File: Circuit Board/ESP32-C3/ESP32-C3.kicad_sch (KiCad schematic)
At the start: 9 parts

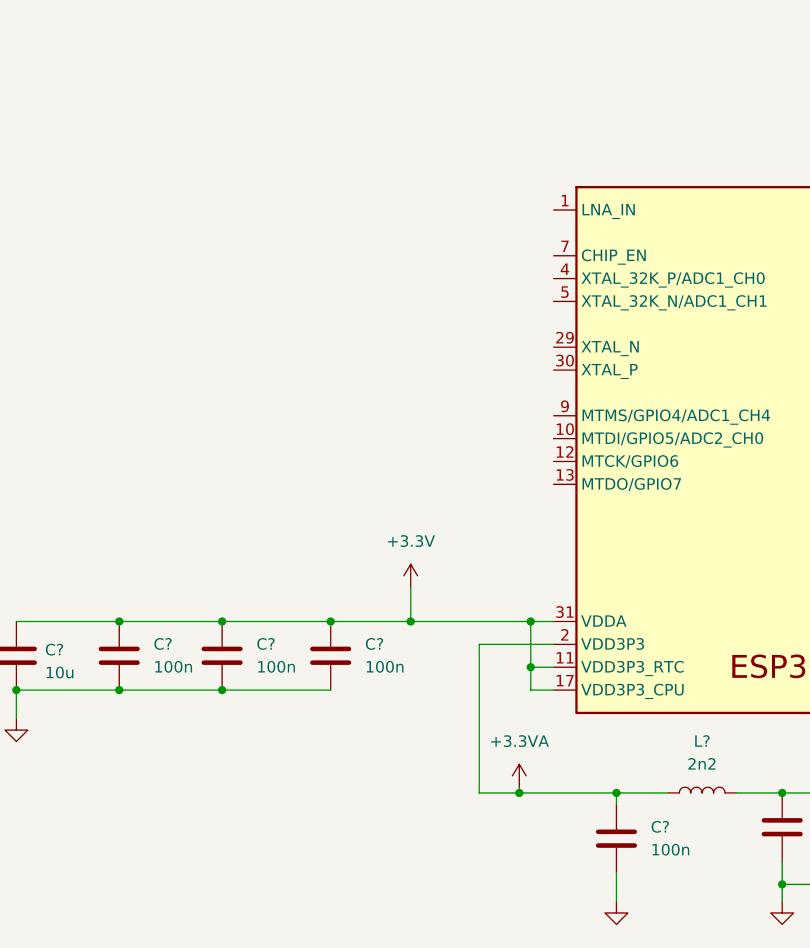
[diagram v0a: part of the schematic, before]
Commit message: Added the crystal oscillator
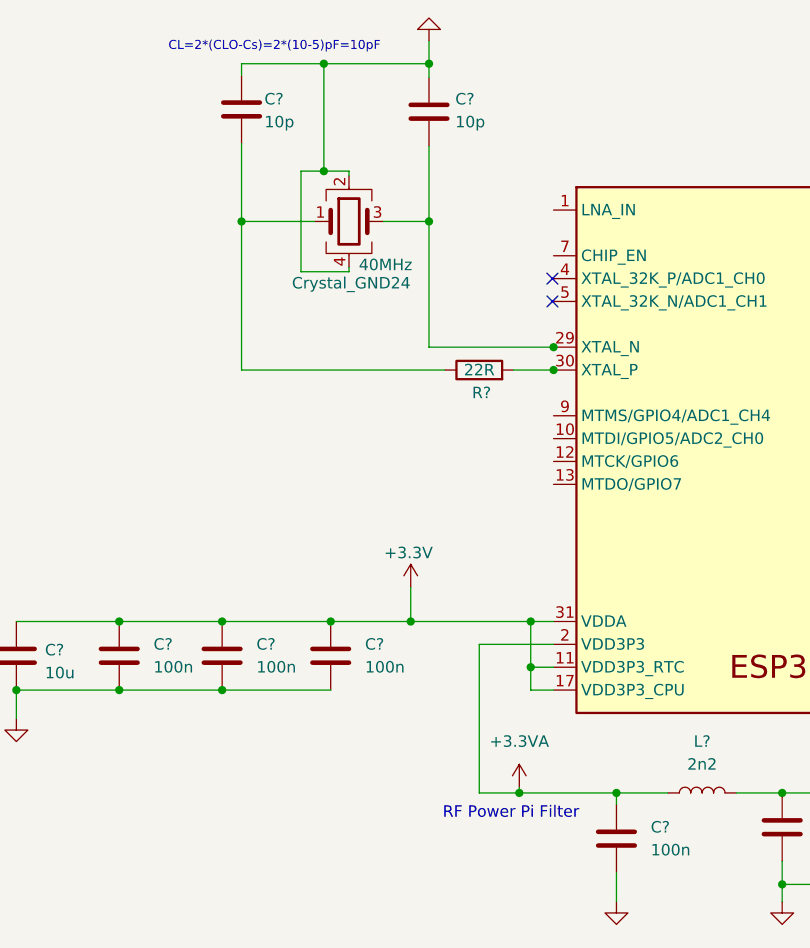
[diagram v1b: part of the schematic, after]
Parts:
- added 40MHz: Crystal_GND24, symbol Device:Crystal_GND24
- added C? (x2): 10p, symbol Device:C
- added R?: 22R, symbol Device:R
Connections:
- net GND: now also 40MHz.2, 40MHz.4, C?.1, C?.1
- net at U?.29 (XTAL_N): now also 40MHz.3, C?.2
- net at U?.30 (XTAL_P): now also R?.2
- new net: 40MHz.1, C?.2, R?.1
- no-connect marks 0 -> 2
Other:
- note added: "CL=2*(CLO-Cs)=2*(10-5)pF=10pF"
- note added: "RF Power Pi Filter"

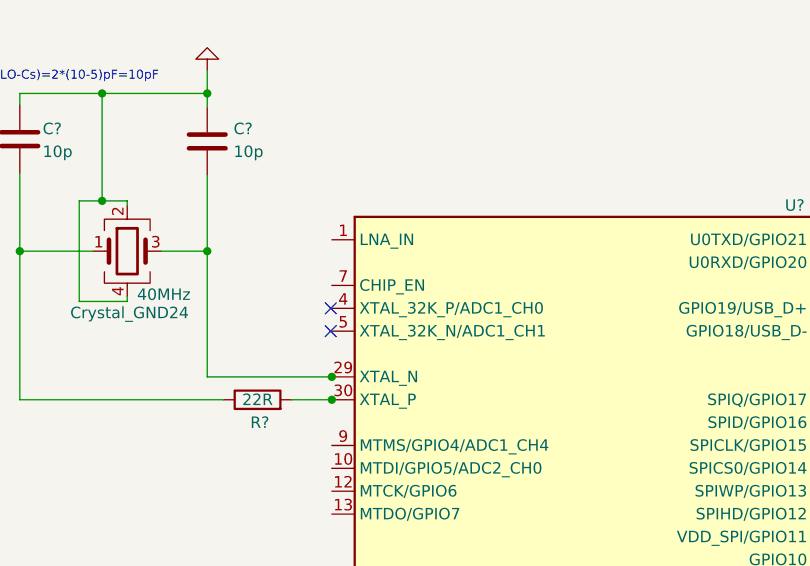
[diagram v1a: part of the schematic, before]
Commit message: Added power on switch
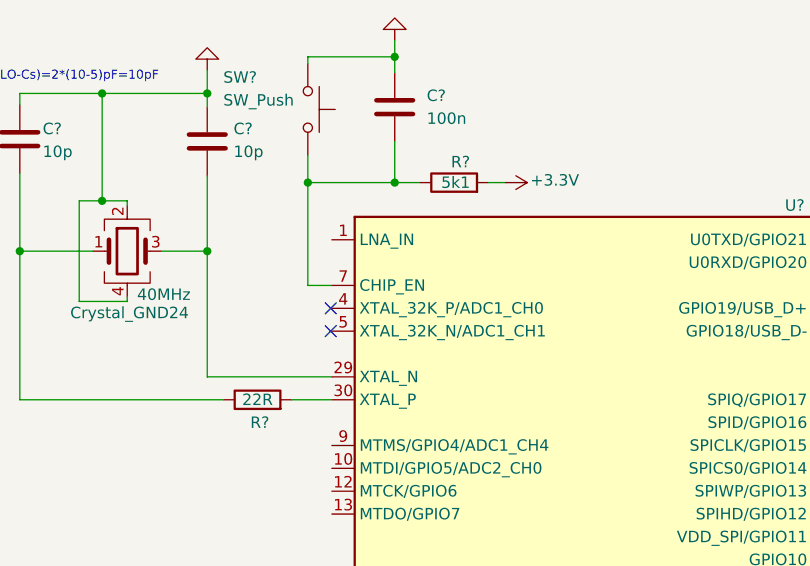
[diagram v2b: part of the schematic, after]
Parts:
- added C?: 100n, symbol Device:C
- added R?: 5k1, symbol Device:R
- added SW?: SW_Push, symbol Switch:SW_Push
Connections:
- net +3.3V: now also R?.2
- net GND: now also C?.1, SW?.1
- net at U?.7 (CHIP_EN): now also C?.2, R?.1, SW?.2
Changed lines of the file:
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@@
   (junction (at 80.264 72.39) (diameter 0) (color 0 0 0 0)
   )
+  (junction (at 121.92 64.77) (diameter 0) (color 0 0 0 0)
+  )
+  (junction (at 121.92 50.8) (diameter 0) (color 0 0 0 0)
+  )
   (junction (at 153.67 135.89) (diameter 0) (color 0 0 0 0)
   )
@@
   (junction (at 112.395 121.92) (diameter 0) (color 0 0 0 0)
   )
-  (junction (at 114.935 88.9) (diameter 0) (color 0 0 0 0)
-  )
   (junction (at 89.408 54.864) (diameter 0) (color 0 0 0 0)
   )
@@
   (junction (at 140.335 146.05) (diameter 0) (color 0 0 0 0)
   )
+  (junction (at 112.268 64.77) (diameter 0) (color 0 0 0 0)
+  )
   (junction (at 112.395 116.84) (diameter 0) (color 0 0 0 0)
   )
   (junction (at 121.92 135.89) (diameter 0) (color 0 0 0 0)
-  )
-  (junction (at 114.935 86.36) (diameter 0) (color 0 0 0 0)
   )
   (junction (at 111.125 135.89) (diameter 0) (color 0 0 0 0)
@@
     (stroke (width 0) (type default) (color 0 0 0 0))
   )
-  (wire (pts (xy 115.062 88.9) (xy 114.935 88.9))
+  (wire (pts (xy 121.92 50.8) (xy 121.92 49.022))
     (stroke (width 0) (type default) (color 0 0 0 0))
   )
@@
     (stroke (width 0) (type default) (color 0 0 0 0))
   )
+  (wire (pts (xy 132.334 64.77) (xy 134.112 64.77))
+    (stroke (width 0) (type default) (color 0 0 0 0))
+  )
+  (wire (pts (xy 112.268 64.77) (xy 112.268 76.2))
+    (stroke (width 0) (type default) (color 0 0 0 0))
+  )
   (wire (pts (xy 99.06 116.84) (xy 99.06 113.03))
     (stroke (width 0) (type default) (color 0 0 0 0))
@@
     (stroke (width 0) (type default) (color 0 0 0 0))
   )
+  (wire (pts (xy 112.268 64.77) (xy 121.92 64.77))
+    (stroke (width 0) (type default) (color 0 0 0 0))
+  )
+  (wire (pts (xy 121.92 64.77) (xy 124.714 64.77))
+    (stroke (width 0) (type default) (color 0 0 0 0))
+  )
   (wire (pts (xy 106.68 119.38) (xy 106.68 135.89))
     (stroke (width 0) (type default) (color 0 0 0 0))
@@
     (stroke (width 0) (type default) (color 0 0 0 0))
   )
+  (wire (pts (xy 112.268 50.8) (xy 121.92 50.8))
+    (stroke (width 0) (type default) (color 0 0 0 0))
+  )
   (wire (pts (xy 111.125 135.89) (xy 121.92 135.89))
     (stroke (width 0) (type default) (color 0 0 0 0))
@@
     (stroke (width 0) (type default) (color 0 0 0 0))
   )
-  (wire (pts (xy 115.062 86.36) (xy 114.935 86.36))
+  (wire (pts (xy 121.92 50.8) (xy 121.92 52.578))
     (stroke (width 0) (type default) (color 0 0 0 0))
   )
@@
     (stroke (width 0) (type default) (color 0 0 0 0))
   )
+  (wire (pts (xy 121.92 60.198) (xy 121.92 64.77))
+    (stroke (width 0) (type default) (color 0 0 0 0))
+  )
   (wire (pts (xy 121.92 144.78) (xy 121.92 147.955))
     (stroke (width 0) (type default) (color 0 0 0 0))
@@
     (stroke (width 0) (type default) (color 0 0 0 0))
   )
+  (wire (pts (xy 112.268 51.562) (xy 112.268 50.8))
+    (stroke (width 0) (type default) (color 0 0 0 0))
+  )
+  (wire (pts (xy 112.268 61.722) (xy 112.268 64.77))
+    (stroke (width 0) (type default) (color 0 0 0 0))
+  )
   (wire (pts (xy 153.67 143.51) (xy 153.67 146.05))
     (stroke (width 0) (type default) (color 0 0 0 0))
@@
   )
   (wire (pts (xy 112.395 116.84) (xy 99.06 116.84))
+    (stroke (width 0) (type default) (color 0 0 0 0))
+  )
+  (wire (pts (xy 112.268 76.2) (xy 114.935 76.2))
     (stroke (width 0) (type default) (color 0 0 0 0))
   )
@@
     (pin "1")
     (pin "2")
+  )
+  (symbol (lib_id "power:+3.3V") (at 134.112 64.77 270) (unit 1)
+    (in_bom yes) (on_board yes)
+    (property "Reference" "#PWR?" (id 0) (at 130.302 64.77 0)
+      (effects (font (size 1.27 1.27)) hide)
+    )
+    (property "Value" "+3.3V" (id 1) (at 139.7 64.516 90))
+    (property "Footprint" "" (id 2) (at 134.112 64.77 0)
+      (effects (font (size 1.27 1.27)) hide)
+    )
+    (property "Datasheet" "" (id 3) (at 134.112 64.77 0)
+      (effects (font (size 1.27 1.27)) hide)
+    )
+    (pin "1")
   )
   (symbol (lib_id "Device:C") (at 153.67 139.7 0) (unit 1)
@@
     (pin "4")
   )
+  (symbol (lib_id "power:GND") (at 121.92 49.022 180) (unit 1)
+    (in_bom yes) (on_board yes) (fields_autoplaced)
+    (property "Reference" "#PWR?" (id 0) (at 121.92 42.672 0)
+      (effects (font (size 1.27 1.27)) hide)
+    )
+    (property "Value" "GND" (id 1) (at 121.92 43.942 0)
+      (effects (font (size 1.27 1.27)) hide)
+    )
+    (property "Footprint" "" (id 2) (at 121.92 49.022 0)
+      (effects (font (size 1.27 1.27)) hide)
+    )
+    (property "Datasheet" "" (id 3) (at 121.92 49.022 0)
+      (effects (font (size 1.27 1.27)) hide)
+    )
+    (pin "1")
+  )
   (symbol (lib_id "power:GND") (at 153.67 148.59 0) (unit 1)
     (in_bom yes) (on_board yes) (fields_autoplaced)
@@
     (pin "1")
   )
+  (symbol (lib_id "Device:C") (at 121.92 56.388 0) (unit 1)
+    (in_bom yes) (on_board yes) (fields_autoplaced)
+    (property "Reference" "C?" (id 0) (at 125.476 55.1179 0)
+      (effects (font (size 1.27 1.27)) (justify left))
+    )
+    (property "Value" "100n" (id 1) (at 125.476 57.6579 0)
+      (effects (font (size 1.27 1.27)) (justify left))
+    )
+    (property "Footprint" "" (id 2) (at 122.8852 60.198 0)
+      (effects (font (size 1.27 1.27)) hide)
+    )
+    (property "Datasheet" "~" (id 3) (at 121.92 56.388 0)
+      (effects (font (size 1.27 1.27)) hide)
+    )
+    (pin "1")
+    (pin "2")
+  )
   (symbol (lib_id "Device:C") (at 55.245 120.65 0) (unit 1)
     (in_bom yes) (on_board yes)
@@
     )
     (property "Datasheet" "~" (id 3) (at 55.245 120.65 0)
+      (effects (font (size 1.27 1.27)) hide)
+    )
+    (pin "1")
+    (pin "2")
+  )
+  (symbol (lib_id "Device:R") (at 128.524 64.77 90) (unit 1)
+    (in_bom yes) (on_board yes)
+    (property "Reference" "R?" (id 0) (at 130.302 62.4841 90)
+      (effects (font (size 1.27 1.27)) (justify left))
+    )
+    (property "Value" "5k1" (id 1) (at 130.302 64.77 90)
+      (effects (font (size 1.27 1.27)) (justify left))
+    )
+    (property "Footprint" "" (id 2) (at 128.524 66.548 90)
+      (effects (font (size 1.27 1.27)) hide)
+    )
+    (property "Datasheet" "~" (id 3) (at 128.524 64.77 0)
       (effects (font (size 1.27 1.27)) hide)
     )
@@
     (pin "2")
   )
+  (symbol (lib_id "Switch:SW_Push") (at 112.268 56.642 270) (unit 1)
+    (in_bom yes) (on_board yes)
+    (property "Reference" "SW?" (id 0) (at 102.87 53.086 90)
+      (effects (font (size 1.27 1.27)) (justify left))
+    )
+    (property "Value" "SW_Push" (id 1) (at 102.87 55.626 90)
+      (effects (font (size 1.27 1.27)) (justify left))
+    )
+    (property "Footprint" "" (id 2) (at 117.348 56.642 0)
+      (effects (font (size 1.27 1.27)) hide)
+    )
+    (property "Datasheet" "~" (id 3) (at 117.348 56.642 0)
+      (effects (font (size 1.27 1.27)) hide)
+    )
+    (pin "1")
+    (pin "2")
+  )
   (sheet_instances
     (path "/" (page "1"))
@@
       (reference "#PWR?") (unit 1) (value "GND") (footprint "")
     )
+    (path "/0bf0adee-68a8-48df-ae9f-495389619cf1"
+      (reference "#PWR?") (unit 1) (value "+3.3V") (footprint "")
+    )
     (path "/2e8d3544-5a04-4724-8bac-f893d7e152f1"
       (reference "#PWR?") (unit 1) (value "GND") (footprint "")
@@
       (reference "#PWR?") (unit 1) (value "GND") (footprint "")
     )
+    (path "/3bb8ef40-4f9c-41ad-8eae-2c8918a73292"
+      (reference "#PWR?") (unit 1) (value "GND") (footprint "")
+    )
     (path "/41906f00-a17a-41e3-a291-e3c925deb9b2"
       (reference "#PWR?") (unit 1) (value "GND") (footprint "")
@@
       (reference "C?") (unit 1) (value "100n") (footprint "")
     )
+    (path "/8da9bf4b-63dc-4151-b04c-885ece191e5f"
+      (reference "C?") (unit 1) (value "100n") (footprint "")
+    )
     (path "/9d2f2aff-7332-4fff-bbe2-dbb171a217dc"
       (reference "C?") (unit 1) (value "10u") (footprint "")
@@
       (reference "R?") (unit 1) (value "22R") (footprint "")
     )
+    (path "/b525a4ae-d297-4d4d-9088-9745ef3985a7"
+      (reference "R?") (unit 1) (value "5k1") (footprint "")
+    )
+    (path "/fe4df71a-c9dd-4482-86ce-3213aba20d79"
+      (reference "SW?") (unit 1) (value "SW_Push") (footprint "")
+    )
     (path "/2a0b3a67-3e1f-4442-ade1-9eea5d2b96f0"

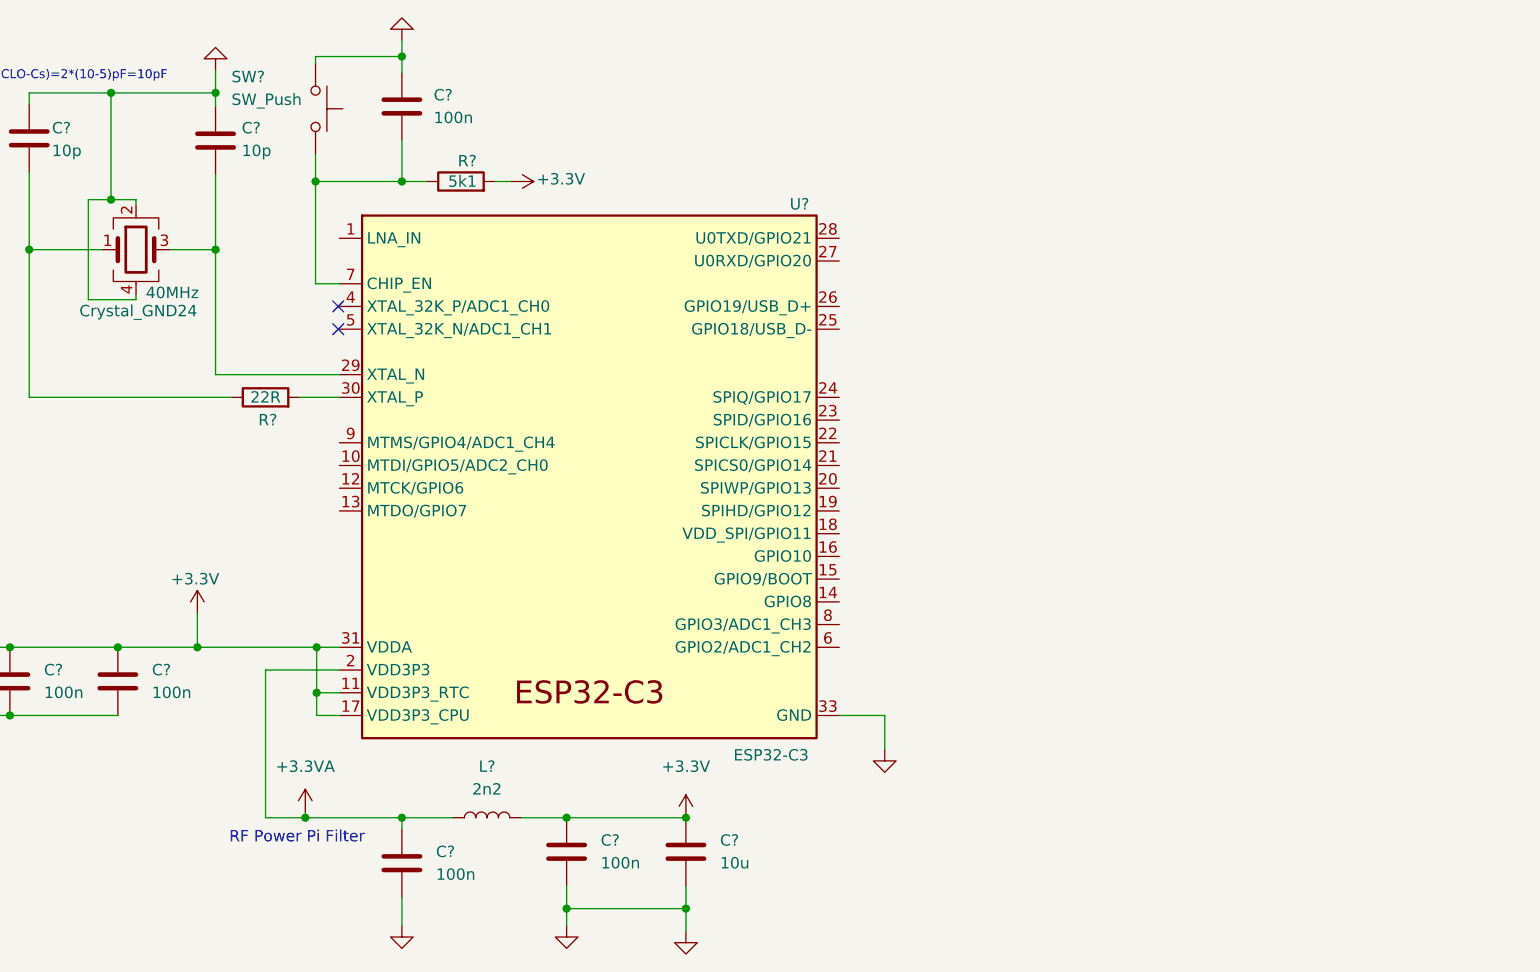
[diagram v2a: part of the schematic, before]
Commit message: Added external flash memory
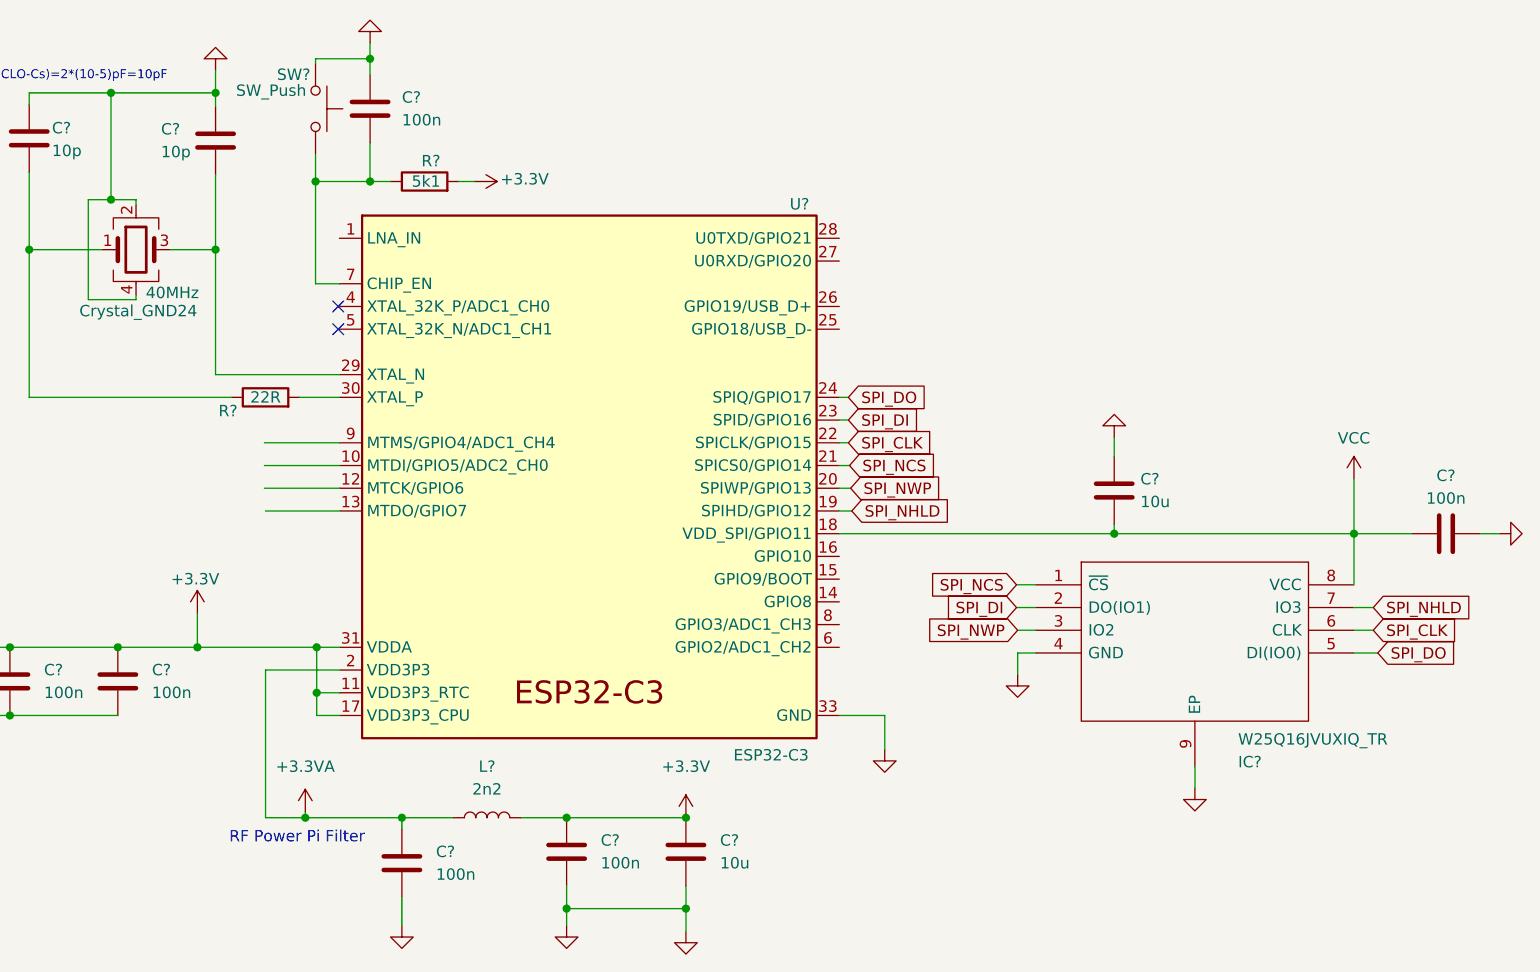
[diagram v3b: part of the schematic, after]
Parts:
- added C?: 10u, symbol Device:C
- added C?: 100n, symbol Device:C
- added IC?: W25Q16JVUXIQ_TR, SON50P300X200X60-9N, symbol W25Q16JVUXIQ_TR:W25Q16JVUXIQ_TR
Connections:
- net GND: now also C?.1, C?.2, IC?.4 (GND), IC?.9 (EP)
- net VCC: now reaches U?.18 (VDD_SPI/GPIO11)
- net VCC: now also C?.1, C?.2, IC?.8 (VCC)
- net SPI_NHLD: now reaches U?.19 (SPIHD/GPIO12)
- net SPI_NHLD: now also IC?.7 (IO3)
- net SPI_NWP: now reaches U?.20 (SPIWP/GPIO13)
- net SPI_NWP: now also IC?.3 (IO2)
- net SPI_NCS: now reaches U?.21 (SPICS0/GPIO14)
- net SPI_NCS: now also IC?.1 (~{CS})
- net SPI_CLK: now reaches U?.22 (SPICLK/GPIO15)
- net SPI_CLK: now also IC?.6 (CLK)
- net SPI_DI: now reaches U?.23 (SPID/GPIO16)
- net SPI_DI: now also IC?.2 (DO(IO1))
- net SPI_DO: now reaches U?.24 (SPIQ/GPIO17)
- net SPI_DO: now also IC?.5 (DI(IO0))
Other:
- moved on the sheet: C?, R?
